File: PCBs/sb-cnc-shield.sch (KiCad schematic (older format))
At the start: 31 parts, among them P10 power switch, P8 12V-36V, Q0 IRF630, SW1 RESET, U1 ARDUINO_UNO_SHIELD/hi five re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, U2 X, U3 Y, U4 Z, U5 A

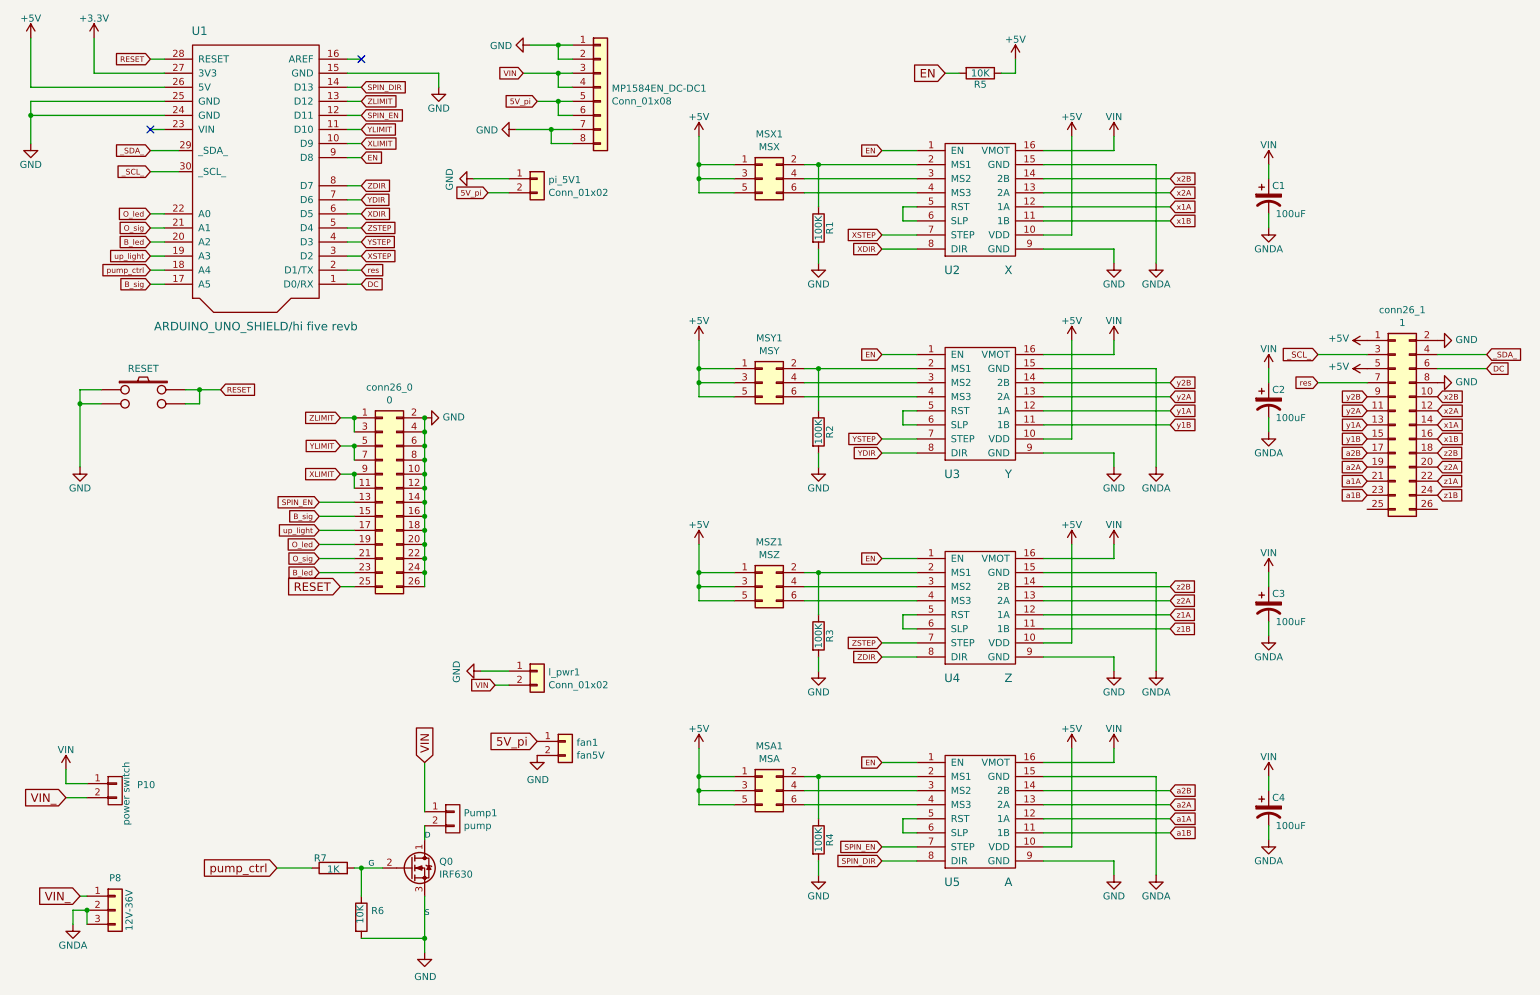
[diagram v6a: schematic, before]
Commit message: add DB25 pinout
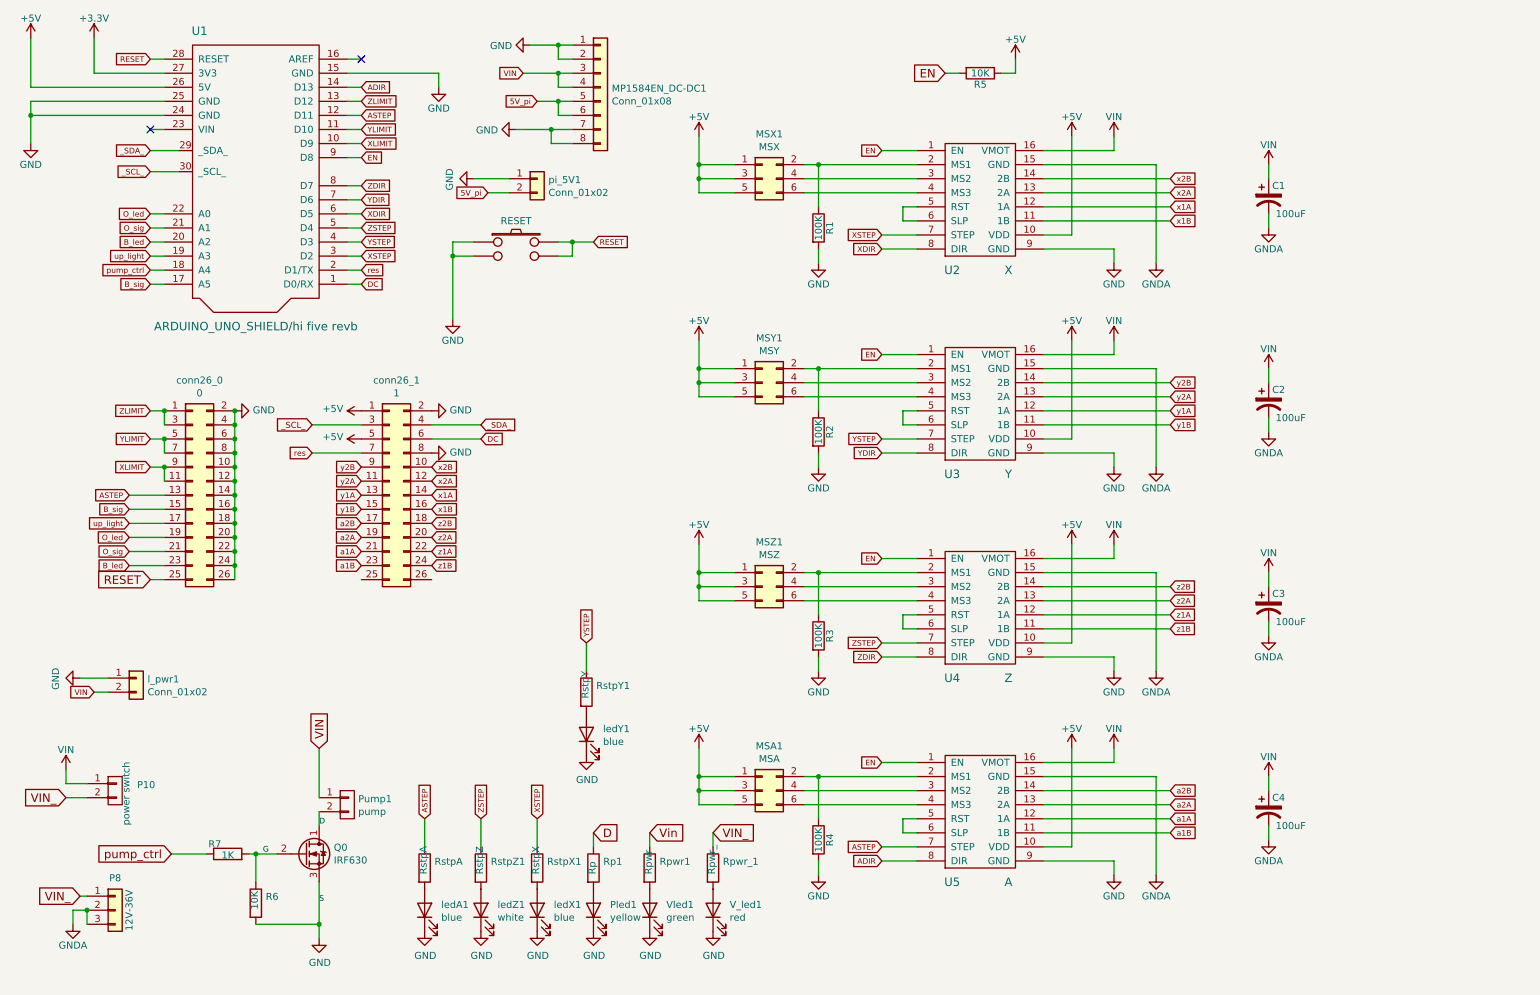
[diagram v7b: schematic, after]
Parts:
- removed fan1: fan5V, Connector_JST:JST_SH_BM02B-SRSS-TB_1x02-1MP_P1.00mm_Vertical, symbol Connector_Generic:Conn_01x02
- added Pled1: yellow, LED_THT:LED_D3.0mm_Horizontal_O1.27mm_Z2.0mm, symbol Device:LED
- added Rp1: Rp, Resistor_SMD:R_0805_2012Metric, symbol Device:R
- added Rpwr1: Rpwr, Resistor_SMD:R_0805_2012Metric, symbol Device:R
- added Rpwr_1: Rpwr_, Resistor_SMD:R_0805_2012Metric, symbol Device:R
- added RstpA: RstpA, Resistor_SMD:R_0805_2012Metric, symbol Device:R
- added RstpX1: RstpX, Resistor_SMD:R_0805_2012Metric, symbol Device:R
- added RstpY1: RstpY, Resistor_SMD:R_0805_2012Metric, symbol Device:R
- added RstpZ1: RstpZ, Resistor_SMD:R_0805_2012Metric, symbol Device:R
- added V_led1: red, LED_THT:LED_D3.0mm_Horizontal_O1.27mm_Z2.0mm, symbol Device:LED
- added Vled1: green, LED_THT:LED_D3.0mm_Horizontal_O1.27mm_Z2.0mm, symbol Device:LED
- added ledA1, ledX1, ledY1: blue, LED_THT:LED_D3.0mm_Horizontal_O1.27mm_Z2.0mm, symbol Device:LED
- added ledZ1: white, LED_THT:LED_D3.0mm_Horizontal_O1.27mm_Z2.0mm, symbol Device:LED
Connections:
- net D: now also Rp1.1
- net GND: now also Pled1.1 (K), V_led1.1 (K), Vled1.1 (K), ledA1.1 (K), ledX1.1 (K), ledY1.1 (K), ledZ1.1 (K)
- net VIN_: now also Rpwr_1.1
- net XSTEP: now also RstpX1.1
- net YSTEP: now also RstpY1.1
- net ZSTEP: now also RstpZ1.1
- net SPIN_DIR renamed ADIR
- net SPIN_EN renamed ASTEP
- net ASTEP: now also RstpA.1
- new net: Pled1.2 (A), Rp1.2
- new net: Rpwr1.2, Vled1.2 (A)
- new net: RstpA.2, ledA1.2 (A)
- new net: Rpwr_1.2, V_led1.2 (A)
- new net: RstpZ1.2, ledZ1.2 (A)
- new net: RstpX1.2, ledX1.2 (A)
- new net: RstpY1.2, ledY1.2 (A)
- new net Vin: Rpwr1.1
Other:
- moved on the sheet: Pump1, Q0, R6, R7, conn26_0, conn26_1, l_pwr1

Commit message: pinout modify
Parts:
- P10: footprint Connector_PinHeader_2.54mm:PinHeader_1x02_P2.54mm_Vertical -> Connector_JST:JST_EH_B2B-EH-A_1x02_P2.50mm_Vertical
- renumbered RstpA to RstpA1
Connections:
- net Vin is gone; now on net VIN: Rpwr1.1
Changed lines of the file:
@@
 F 0 "P10" H 1356 6191 50  0000 L CNN
 F 1 "power switch" V 1278 5903 50  0000 L CNN
-F 2 "Connector_PinHeader_2.54mm:PinHeader_1x02_P2.54mm_Vertical" H 1200 6150 50  0001 C CNN
+F 2 "Connector_JST:JST_EH_B2B-EH-A_1x02_P2.50mm_Vertical" H 1200 6150 50  0001 C CNN
 F 3 "" H 1200 6150 50  0000 C CNN
 	1    1200 6150
@@
 	5000 6550 5000 6450
 Text GLabel 5000 6450 2    60   Input ~ 0
-Vin
+VIN
 $Comp
 L Device:LED ledA1
@@
 $EndComp
 $Comp
-L Device:R RstpA
+L Device:R RstpA1
 U 1 1 61C24B31
 P 3400 6700
-F 0 "RstpA" H 3470 6746 50  0000 L CNN
+F 0 "RstpA1" H 3470 6746 50  0000 L CNN
 F 1 "RstpA" V 3391 6655 50  0000 L CNN
 F 2 "Resistor_SMD:R_0805_2012Metric" V 3330 6700 50  0001 C CNN
